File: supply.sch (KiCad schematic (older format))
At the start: 79 parts, among them IC1 TPS54561, J10 61300311121, J3 DC_SOCKET, U10 LM3881MME_NOPB, U4 TPS65296, U5 TPS62823DLCT, U9 TPS62823DLCT

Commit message: Update local libraries
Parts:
- C100: footprint antmicro-footprints:0603-cap -> lpddr4-test-board-footprints:0603-cap; symbol antmicroCapacitors0603:C_10n_0603 -> lpddr4-test-board:C_10n_0603
- C101: footprint antmicro-footprints:0402-cap -> lpddr4-test-board-footprints:0402-cap; symbol lpddr4-test-board-rescue:C_100n_0402_6V3-antmicroCapacitors0402 -> lpddr4-test-board:C_100n_0402_6V3-antmicroCapacitors0402
- C97: footprint antmicro-footprints:0603-cap -> lpddr4-test-board-footprints:0603-cap; symbol antmicroCapacitors0603:C_4u7_0603 -> lpddr4-test-board:C_4u7_0603
- R35: footprint antmicro-footprints:0402-res -> lpddr4-test-board-footprints:0402-res; symbol antmicroResistors0402:R_5R1_0402 -> lpddr4-test-board:R_5R1_0402
- R45: footprint antmicro-footprints:0402-res -> lpddr4-test-board-footprints:0402-res; symbol antmicroResistors0402:R_453k_0402 -> lpddr4-test-board:R_453k_0402
- R46: footprint antmicro-footprints:0402 -> lpddr4-test-board-footprints:0402; symbol antmicroResistors0402:R_100k_1%_0402 -> lpddr4-test-board:R_100k_1%_0402
- R48: footprint antmicro-footprints:0603-res -> lpddr4-test-board-footprints:0603-res; symbol antmicroResistors0603:R_66k5_0603 -> lpddr4-test-board:R_66k5_0603
- R49: footprint antmicro-footprints:0603-res -> lpddr4-test-board-footprints:0603-res; symbol antmicroResistors0603:R_100k_0603 -> lpddr4-test-board:R_100k_0603
- R55: footprint antmicro-footprints:0402-res -> lpddr4-test-board-footprints:0402-res; symbol antmicroResistors0402:R_0R_0402 -> lpddr4-test-board:R_0R_0402
- U10: footprint antmicro-footprints:VSSOP8-Texas_Instruments-DGK0008A -> lpddr4-test-board-footprints:VSSOP8-Texas_Instruments-DGK0008A; symbol antmicroPMICVoltageRegulatorsDCDCSwitchingControllers:LM3881MME_NOPB -> lpddr4-test-board:LM3881MME_NOPB
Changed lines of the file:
@@
 $EndComp
 $Comp
-L antmicroResistors0402:R_5R1_0402 R35
+L lpddr4-test-board:R_5R1_0402 R35
 U 1 1 609CC1B7
 P 4475 2275
 F 0 "R35" H 4300 2375 60  0000 C CNN
 F 1 "R_5R1_0402" H 4475 2125 60  0001 C CNN
-F 2 "antmicro-footprints:0402-res" H 4675 2475 60  0001 L CNN
+F 2 "lpddr4-test-board-footprints:0402-res" H 4675 2475 60  0001 L CNN
 F 3 "" H 4475 2275 50  0001 C CNN
 F 4 "PANASONIC" H 4675 2675 60  0001 L CNN "Manufacturer"
@@
 	5475 9775 6300 9775
 $Comp
-L antmicroResistors0603:R_66k5_0603 R48
+L lpddr4-test-board:R_66k5_0603 R48
 U 1 1 5FE2DA05
 P 8100 9775
 F 0 "R48" V 8055 9845 60  0000 L CNN
 F 1 "R_66k5_0603" H 8100 9625 60  0001 C CNN
-F 2 "antmicro-footprints:0603-res" H 8300 9975 60  0001 L CNN
+F 2 "lpddr4-test-board-footprints:0603-res" H 8300 9975 60  0001 L CNN
 F 3 "" H 8100 9775 50  0001 C CNN
 F 4 "PANASONIC_ELECTRONIC_COMPONENTS" H 8300 10175 60  0001 L CNN "Manufacturer"
@@
 $EndComp
 $Comp
-L antmicroResistors0603:R_100k_0603 R49
+L lpddr4-test-board:R_100k_0603 R49
 U 1 1 5FE2EB23
 P 8100 10075
 F 0 "R49" V 8055 10145 60  0000 L CNN
 F 1 "R_100k_0603" H 8100 9925 60  0001 C CNN
-F 2 "antmicro-footprints:0603-res" H 8300 10275 60  0001 L CNN
+F 2 "lpddr4-test-board-footprints:0603-res" H 8300 10275 60  0001 L CNN
 F 3 "" H 8100 10075 50  0001 C CNN
 F 4 "BOURNS" H 8300 10475 60  0001 L CNN "Manufacturer"
@@
 Connection ~ 8100 9925
 $Comp
-L antmicroResistors0402:R_453k_0402 R45
+L lpddr4-test-board:R_453k_0402 R45
 U 1 1 5FE38DF2
 P 4150 9800
 F 0 "R45" V 4105 9870 60  0000 L CNN
 F 1 "R_453k_0402" H 4150 9650 60  0001 C CNN
-F 2 "antmicro-footprints:0402-res" H 4350 10000 60  0001 L CNN
+F 2 "lpddr4-test-board-footprints:0402-res" H 4350 10000 60  0001 L CNN
 F 3 "" H 4150 9800 50  0001 C CNN
 F 4 "VISHAY" H 4350 10200 60  0001 L CNN "Manufacturer"
@@
 $EndComp
 $Comp
-L antmicroResistors0402:R_100k_1%_0402 R46
+L lpddr4-test-board:R_100k_1%_0402 R46
 U 1 1 5FE39D9C
 P 4150 10100
 F 0 "R46" V 4105 10170 60  0000 L CNN
 F 1 "R_100k_1%_0402" H 4150 9950 60  0001 C CNN
-F 2 "antmicro-footprints:0402" H 4350 10300 60  0001 L CNN
+F 2 "lpddr4-test-board-footprints:0402" H 4350 10300 60  0001 L CNN
 F 3 "" H 4150 10100 50  0001 C CNN
 F 4 "PANASONIC" H 4350 10500 60  0001 L CNN "Manufacturer"
@@
 Connection ~ 4150 9950
 $Comp
-L antmicroCapacitors0603:C_4u7_0603 C97
+L lpddr4-test-board:C_4u7_0603 C97
 U 1 1 5FE45523
 P 5975 10075
 F 0 "C97" H 5725 10100 60  0000 L CNN
 F 1 "C_4u7_0603" H 5975 9925 60  0001 C CNN
-F 2 "antmicro-footprints:0603-cap" H 6175 10275 60  0001 L CNN
+F 2 "lpddr4-test-board-footprints:0603-cap" H 6175 10275 60  0001 L CNN
 F 3 "" H 5975 10075 50  0001 C CNN
 F 4 "TDK" H 6175 10475 60  0001 L CNN "Manufacturer"
@@
 	7800 6250 7800 5875
 $Comp
-L lpddr4-test-board-rescue:C_100n_0402_6V3-antmicroCapacitors0402 C101
+L lpddr4-test-board:C_100n_0402_6V3-antmicroCapacitors0402 C101
 U 1 1 5FE75452
 P 9800 5700
@@
 F 0 "C101" H 9915 5745 60  0000 L CNN
 F 1 "C_100n_0402_6V3" H 9800 5550 60  0001 C CNN
-F 2 "antmicro-footprints:0402-cap" H 10000 5900 60  0001 L CNN
+F 2 "lpddr4-test-board-footprints:0402-cap" H 10000 5900 60  0001 L CNN
 F 3 "" H 9800 5700 50  0001 C CNN
 F 4 "Walsin" H 10000 6100 60  0001 L CNN "Manufacturer"
@@
 	7775 6350 8250 6350
 $Comp
-L antmicroPMICVoltageRegulatorsDCDCSwitchingControllers:LM3881MME_NOPB U10
+L lpddr4-test-board:LM3881MME_NOPB U10
 U 1 1 5FE68F88
 P 8650 6350
 F 0 "U10" H 8650 6843 60  0000 C CNN
 F 1 "LM3881MME_NOPB" H 8400 6000 60  0001 L CNN
-F 2 "antmicro-footprints:VSSOP8-Texas_Instruments-DGK0008A" H 8850 6550 60  0001 L CNN
+F 2 "lpddr4-test-board-footprints:VSSOP8-Texas_Instruments-DGK0008A" H 8850 6550 60  0001 L CNN
 F 3 "https://www.ti.com/lit/ds/symlink/lm3881.pdf?ts=1607507933694&ref_url=https%253A%252F%252Fwww.ti.com%252Fpower-management%252Fsequencers%252Fproducts.html" H 8850 6650 60  0001 L CNN
 F 4 "Texas Instruments" H 8650 6737 60  0000 C CNN "Manufacturer"
@@
 VCC_IO_EN
 $Comp
-L antmicroResistors0402:R_0R_0402 R55
+L lpddr4-test-board:R_0R_0402 R55
 U 1 1 5FEBD15D
 P 8050 6750
 F 0 "R55" V 8005 6820 60  0000 L CNN
 F 1 "R_0R_0402" H 8050 6600 60  0001 C CNN
-F 2 "antmicro-footprints:0402-res" H 8250 6950 60  0001 L CNN
+F 2 "lpddr4-test-board-footprints:0402-res" H 8250 6950 60  0001 L CNN
 F 3 "" H 8050 6750 50  0001 C CNN
 F 4 "PANASONIC" H 8250 7150 60  0001 L CNN "Manufacturer"
@@
 STEP1 - VCCINT   (1.0V) for FPGA\nSTEP2 - VCCAUX (1.8V, 1.1V) for FPGA and DDR\nSTEP3 - VCCIO     (3.3V, 1.1V) for FPGA and DDR
 $Comp
-L antmicroCapacitors0603:C_10n_0603 C100
+L lpddr4-test-board:C_10n_0603 C100
 U 1 1 5FEE4E91
 P 7700 6700
 F 0 "C100" H 7585 6655 60  0000 R CNN
 F 1 "C_10n_0603" H 7700 6550 60  0001 C CNN
-F 2 "antmicro-footprints:0603-cap" H 7900 6900 60  0001 L CNN
+F 2 "lpddr4-test-board-footprints:0603-cap" H 7900 6900 60  0001 L CNN
 F 3 "" H 7700 6700 50  0001 C CNN
 F 4 "AVX" H 7900 7100 60  0001 L CNN "Manufacturer"

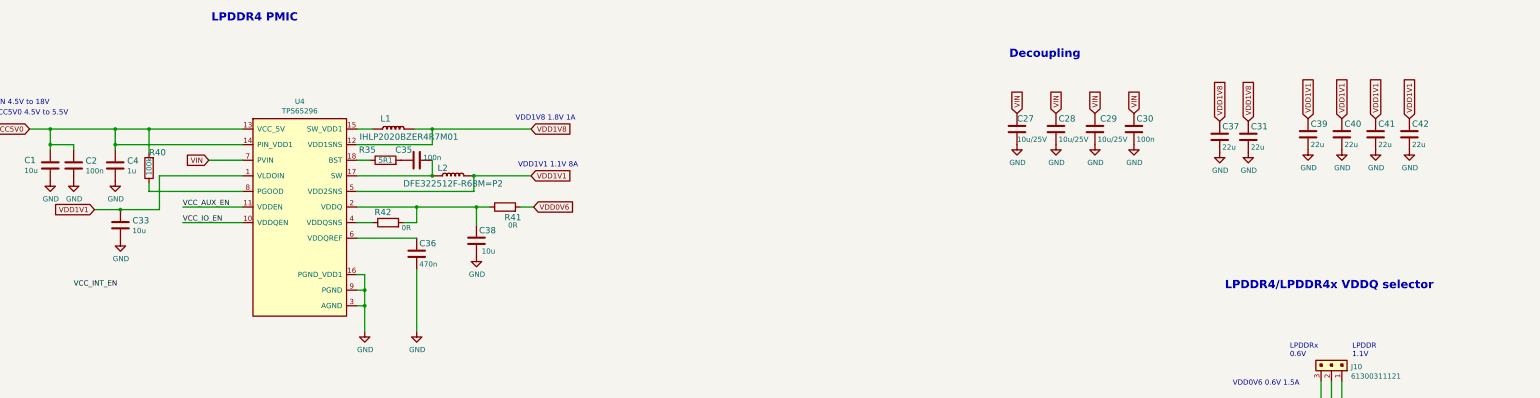
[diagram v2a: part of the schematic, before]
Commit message: Add VCC1 plane decoupling capacitors
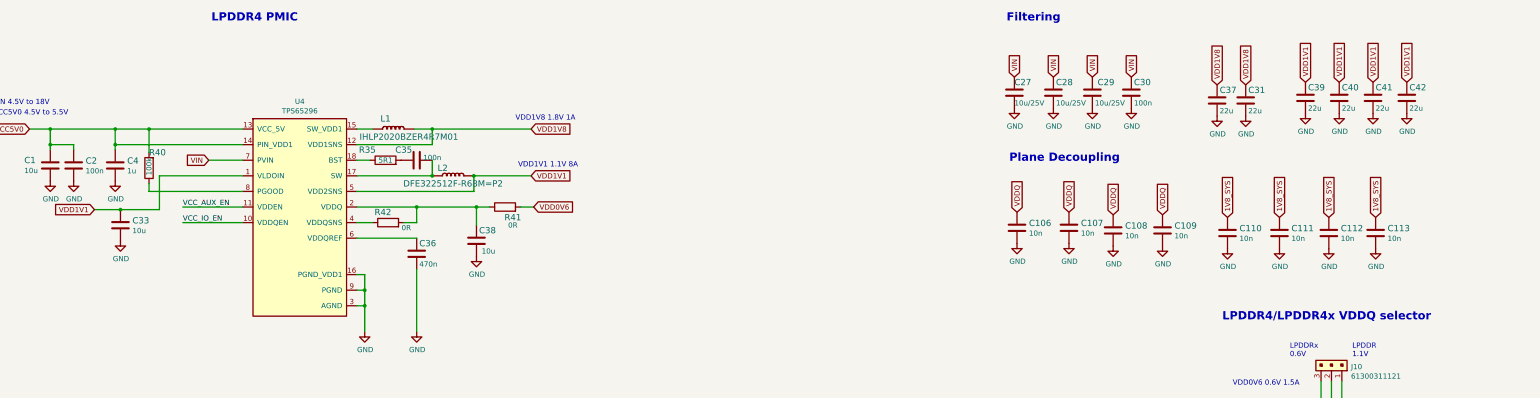
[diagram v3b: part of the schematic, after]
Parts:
- added C106, C107, C108, C109, C110, C111, C112, C113: C_10n_0603, antmicro-footprints:0603-cap, symbol antmicroCapacitors0603:C_10n_0603
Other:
- note added: "Filtering"
- note added: "Plane Decoupling"
- note removed: "Decoupling"
- moved on the sheet: C27, C28, C29, C30, C31, C37, C39, C40, C41, C42

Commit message: Add slide switch with labels
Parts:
- removed C165, C167, C170: C_2u2_0402, lpddr4-test-board-footprints:0402-cap, symbol lpddr4-test-board:C_2u2_0402
- added C116, C117, C118: C_47u_16V_1206, antmicro-footprints:1206-cap, symbol antmicroCapacitorsmisc:C_47u_16V_1206
- added S1: EG1218, antmicro-footprints:Switch_Slide_11.6x4mm_EG1218, symbol antmicroSlideSwitches:EG1218
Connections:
- net labels added: SYS_EN
- wire segments 154 -> 157
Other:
- note added: "Power switch"
- note removed: "Enabled by default"
- note removed: "TODO: add power slide switch"
- moved on the sheet: TP9
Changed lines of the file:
@@
-$EndComp
-$Comp
-L lpddr4-test-board:C_2u2_0402 C165
-U 1 1 603D3854
-P 1100 6700
-F 0 "C165" H 1125 6800 60  0000 L CNN
-F 1 "C_2u2_0402" H 1100 6550 60  0001 C CNN
-F 2 "lpddr4-test-board-footprints:0402-cap" H 1300 6900 60  0001 L CNN
-F 3 "" H 1100 6700 50  0001 C CNN
-F 4 "TDK" H 1300 7100 60  0001 L CNN "Manufacturer"
-F 5 "C1005X5R1A225K050BC" H 1300 7000 60  0001 L CNN "MPN"
-F 6 "2u2" H 1125 6625 50  0000 L CNN "Val"
-	1    1100 6700
-	1    0    0    -1
-$EndComp
-$Comp
-L lpddr4-test-board:C_2u2_0402 C167
-U 1 1 603D3E2F
-P 1400 6700
-F 0 "C167" H 1425 6800 60  0000 L CNN
-F 1 "C_2u2_0402" H 1400 6550 60  0001 C CNN
-F 2 "lpddr4-test-board-footprints:0402-cap" H 1600 6900 60  0001 L CNN
-F 3 "" H 1400 6700 50  0001 C CNN
-F 4 "TDK" H 1600 7100 60  0001 L CNN "Manufacturer"
-F 5 "C1005X5R1A225K050BC" H 1600 7000 60  0001 L CNN "MPN"
-F 6 "2u2" H 1425 6625 50  0000 L CNN "Val"
-	1    1400 6700
-	1    0    0    -1
-$EndComp
-$Comp
-L lpddr4-test-board:C_2u2_0402 C170
-U 1 1 603D43CA
-P 1700 6700
-F 0 "C170" H 1725 6800 60  0000 L CNN
-F 1 "C_2u2_0402" H 1700 6550 60  0001 C CNN
-F 2 "lpddr4-test-board-footprints:0402-cap" H 1900 6900 60  0001 L CNN
-F 3 "" H 1700 6700 50  0001 C CNN
-F 4 "TDK" H 1900 7100 60  0001 L CNN "Manufacturer"
-F 5 "C1005X5R1A225K050BC" H 1900 7000 60  0001 L CNN "MPN"
-F 6 "2u2" H 1725 6625 50  0000 L CNN "Val"
-	1    1700 6700
-	1    0    0    -1
 $EndComp
 $Comp
 L lpddr4-test-board:GND #PWR0189
 U 1 1 603D4A1C
-P 1100 6850
-F 0 "#PWR0189" H 1100 6600 50  0001 C CNN
-F 1 "GND" H 1105 6677 50  0000 C CNN
-F 2 "" H 1100 6850 50  0001 C CNN
-F 3 "" H 1100 6850 50  0001 C CNN
-	1    1100 6850
+P 1000 5450
+F 0 "#PWR0189" H 1000 5200 50  0001 C CNN
+F 1 "GND" H 1005 5277 50  0000 C CNN
+F 2 "" H 1000 5450 50  0001 C CNN
+F 3 "" H 1000 5450 50  0001 C CNN
+	1    1000 5450
 	1    0    0    -1
 $EndComp
@@
 L lpddr4-test-board:GND #PWR0190
 U 1 1 603D4F8F
-P 1400 6850
-F 0 "#PWR0190" H 1400 6600 50  0001 C CNN
-F 1 "GND" H 1405 6677 50  0000 C CNN
-F 2 "" H 1400 6850 50  0001 C CNN
-F 3 "" H 1400 6850 50  0001 C CNN
-	1    1400 6850
+P 1575 5450
+F 0 "#PWR0190" H 1575 5200 50  0001 C CNN
+F 1 "GND" H 1580 5277 50  0000 C CNN
+F 2 "" H 1575 5450 50  0001 C CNN
+F 3 "" H 1575 5450 50  0001 C CNN
+	1    1575 5450
 	1    0    0    -1
 $EndComp
@@
 L lpddr4-test-board:GND #PWR0191
 U 1 1 603D54DC
-P 1700 6850
-F 0 "#PWR0191" H 1700 6600 50  0001 C CNN
-F 1 "GND" H 1705 6677 50  0000 C CNN
-F 2 "" H 1700 6850 50  0001 C CNN
-F 3 "" H 1700 6850 50  0001 C CNN
-	1    1700 6850
+P 2150 5450
+F 0 "#PWR0191" H 2150 5200 50  0001 C CNN
+F 1 "GND" H 2155 5277 50  0000 C CNN
+F 2 "" H 2150 5450 50  0001 C CNN
+F 3 "" H 2150 5450 50  0001 C CNN
+	1    2150 5450
 	1    0    0    -1
 $EndComp
@@
 Text GLabel 2500 5700 1    50   Input ~ 0
 VIN
-Text GLabel 1100 6550 1    50   Input ~ 0
+Text GLabel 1000 5150 1    50   Input ~ 0
 VIN
-Text GLabel 1400 6550 1    50   Input ~ 0
+Text GLabel 1575 5150 1    50   Input ~ 0
 VIN
-Text GLabel 1700 6550 1    50   Input ~ 0
+Text GLabel 2150 5150 1    50   Input ~ 0
 VIN
 $Comp
@@
 L lpddr4-test-board:TP_SMD1MM TP9
 U 1 1 6C3554ED
-P 2275 6150
-F 0 "TP9" V 2180 6197 50  0000 C CNN
-F 1 "TP_SMD1MM" H 2275 6050 50  0001 C CNN
-F 2 "lpddr4-test-board-footprints:Testpoint_smd_1mm" H 2475 6350 60  0001 L CNN
-F 3 "" H 2475 6450 60  0001 L CNN
-	1    2275 6150
+P 2125 6150
+F 0 "TP9" V 2125 6025 50  0000 C CNN
+F 1 "TP_SMD1MM" H 2125 6050 50  0001 C CNN
+F 2 "lpddr4-test-board-footprints:Testpoint_smd_1mm" H 2325 6350 60  0001 L CNN
+F 3 "" H 2325 6450 60  0001 L CNN
+	1    2125 6150
 	0    1    1    0
 $EndComp
@@
 	8050 6550 8050 6600
 Wire Wire Line
-	2375 6150 2650 6150
-Text Notes 1350 6175 0    59   ~ 0
-Enabled by default
+	2225 6150 2650 6150
 Text Notes 9275 6850 0    47   ~ 0
 STEP1 - VCCINT   (1.0V) for FPGA\nSTEP2 - VCCAUX (1.8V, 1.1V) for FPGA and DDR\nSTEP3 - VCCIO     (3.3V, 1.1V) for FPGA and DDR
@@
 VCC_IO_EN
 Text Notes 9400 8150 0    79   ~ 16
-TODO: add power slide switch
+Power switch
 $Comp
 L lpddr4-test-board:GND #PWR014
@@
 	1    0    0    -1
 $EndComp
+$Comp
+L antmicroSlideSwitches:EG1218 S1
+U 1 1 602873C2
+P 10350 8725
+F 0 "S1" H 10350 9006 50  0000 C CNN
+F 1 "EG1218" H 10350 8915 50  0000 C CNN
+F 2 "antmicro-footprints:Switch_Slide_11.6x4mm_EG1218" H 10550 8925 50  0001 L CNN
+F 3 "http://spec_sheets.e-switch.com/specs/P040040.pdf" H 10550 9025 60  0001 L CNN
+F 4 "EG1218" H 10550 9225 60  0001 L CNN "MPN"
+F 5 "E-Switch" H 10550 9825 60  0001 L CNN "Manufacturer"
+	1    10350 8725
+	1    0    0    -1
+$EndComp
+Text Label 2250 6150 0    50   ~ 0
+SYS_EN
+Text Label 9675 8725 0    50   ~ 0
+SYS_EN
+Wire Wire Line
+	10150 8725 9525 8725
+$Comp
+L lpddr4-test-board:GND #PWR035
+U 1 1 602A0B72
+P 10675 9000
+F 0 "#PWR035" H 10675 8750 50  0001 C CNN
+F 1 "GND" H 10680 8827 50  0000 C CNN
+F 2 "" H 10675 9000 50  0001 C CNN
+F 3 "" H 10675 9000 50  0001 C CNN
+	1    10675 9000
+	1    0    0    -1
+$EndComp
+Wire Wire Line
+	10550 8825 10675 8825
+Wire Wire Line
+	10675 8825 10675 9000
+$Comp
+L antmicroCapacitorsmisc:C_47u_16V_1206 C116
+U 1 1 602EDD65
+P 1000 5300
+F 0 "C116" H 1115 5345 60  0000 L CNN
+F 1 "C_47u_16V_1206" H 1000 5150 60  0001 C CNN
+F 2 "antmicro-footprints:1206-cap" H 1200 5500 60  0001 L CNN
+F 3 "" H 1000 5300 50  0001 C CNN
+F 4 "TDK" H 1200 5700 60  0001 L CNN "Manufacturer"
+F 5 "C3216X5R1C476M160AB" H 1200 5600 60  0001 L CNN "MPN"
+F 6 "47u/16V" H 1115 5247 50  0000 L CNN "Val"
+	1    1000 5300
+	1    0    0    -1
+$EndComp
+$Comp
+L antmicroCapacitorsmisc:C_47u_16V_1206 C117
+U 1 1 602EFA5A
+P 1575 5300
+F 0 "C117" H 1690 5345 60  0000 L CNN
+F 1 "C_47u_16V_1206" H 1575 5150 60  0001 C CNN
+F 2 "antmicro-footprints:1206-cap" H 1775 5500 60  0001 L CNN
+F 3 "" H 1575 5300 50  0001 C CNN
+F 4 "TDK" H 1775 5700 60  0001 L CNN "Manufacturer"
+F 5 "C3216X5R1C476M160AB" H 1775 5600 60  0001 L CNN "MPN"
+F 6 "47u/16V" H 1690 5247 50  0000 L CNN "Val"
+	1    1575 5300
+	1    0    0    -1
+$EndComp
+$Comp
+L antmicroCapacitorsmisc:C_47u_16V_1206 C118
+U 1 1 602EFC89
+P 2150 5300
+F 0 "C118" H 2265 5345 60  0000 L CNN
+F 1 "C_47u_16V_1206" H 2150 5150 60  0001 C CNN
+F 2 "antmicro-footprints:1206-cap" H 2350 5500 60  0001 L CNN
+F 3 "" H 2150 5300 50  0001 C CNN
+F 4 "TDK" H 2350 5700 60  0001 L CNN "Manufacturer"
+F 5 "C3216X5R1C476M160AB" H 2350 5600 60  0001 L CNN "MPN"
+F 6 "47u/16V" H 2265 5247 50  0000 L CNN "Val"
+	1    2150 5300
+	1    0    0    -1
+$EndComp

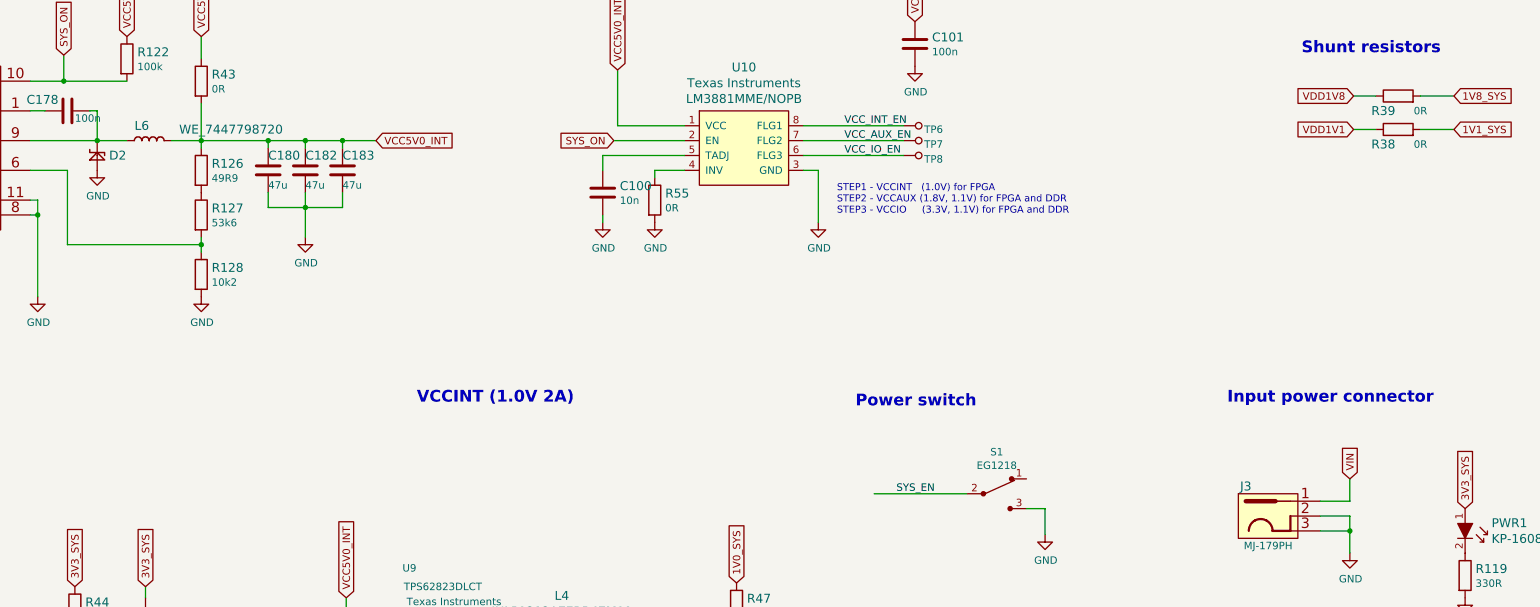
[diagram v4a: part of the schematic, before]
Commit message: Add Schottky protection to VIN
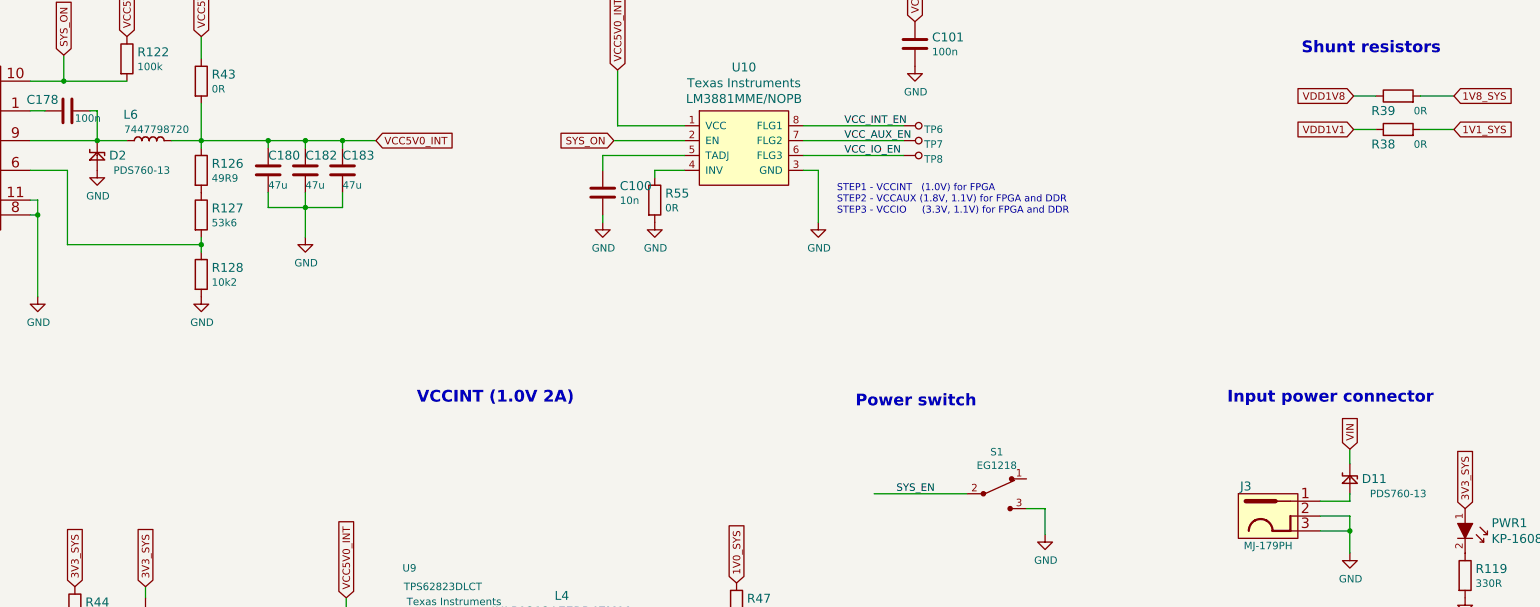
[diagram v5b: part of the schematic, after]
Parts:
- added D11: PDS760-13, lpddr4-test-board-footprints:PDS760-13, symbol lpddr4-test-board:PDS760-13
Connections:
- net VIN: now also D11.C; no longer J3.1
- new net: D11.A, J3.1
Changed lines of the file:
@@
 U 1 1 602EF283
 P 4650 6350
-F 0 "L6" H 4600 6450 60  0000 C CNN
-F 1 "WE_7447798720" H 5200 6425 60  0000 C CNN
+F 0 "L6" H 4525 6525 60  0000 C CNN
+F 1 "WE_7447798720" H 5200 6425 60  0001 C CNN
 F 2 "lpddr4-test-board-footprints:WE_7447798720" H 4700 6200 60  0001 C CNN
 F 3 "" H 4705 6380 60  0001 C CNN
 F 4 "Wurth Elektronik" H 4650 6250 50  0001 C CNN "Manufacturer"
-F 5 "7447798720" H 4600 6300 50  0001 C CNN "MPN"
+F 5 "7447798720" H 4700 6425 50  0000 C CNN "MPN"
 	1    4650 6350
 	1    0    0    -1
@@
 F 3 "" H 4300 6450 60  0001 C CNN
 F 4 "Diodes Inc." H 4300 6450 50  0001 C CNN "Manufacturer"
-F 5 "PDS760-13" H 4300 6450 50  0001 C CNN "MPN"
+F 5 "PDS760-13" H 4600 6350 50  0000 C CNN "MPN"
 	1    4300 6450
 	1    0    0    -1
@@
 	1    0    0    -1
 $EndComp
-Text GLabel 12725 8625 1    50   Input ~ 0
+Text GLabel 12725 8425 1    50   Input ~ 0
 VIN
 Wire Wire Line
 	12525 8775 12725 8775
 Wire Wire Line
-	12725 8775 12725 8625
+	12725 8775 12725 8725
 Wire Wire Line
 	12525 8875 12725 8875
@@
 	1    0    0    -1
 $EndComp
+$Comp
+L lpddr4-test-board:PDS760-13 D11
+U 1 1 6034544D
+P 12725 8625
+F 0 "D11" H 12805 8625 60  0000 L CNN
+F 1 "PDS760-13" H 12825 8525 60  0001 L BNN
+F 2 "lpddr4-test-board-footprints:PDS760-13" H 12725 8625 60  0001 C CNN
+F 3 "" H 12725 8625 60  0001 C CNN
+F 4 "Diodes Inc." H 12725 8625 50  0001 C CNN "Manufacturer"
+F 5 "PDS760-13" H 13050 8525 50  0000 C CNN "MPN"
+	1    12725 8625
+	1    0    0    -1
+$EndComp
+Wire Wire Line
+	12725 8425 12725 8525
 $EndSCHEMATC
